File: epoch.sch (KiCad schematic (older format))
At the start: 30 parts, among them J1 USB_OTG, J2 CONN_01X05, P3 CONN_01X10, Q1 DMP1045U, SW1 SW_Reset, SW2 SW_Up, SW3 SW_Middle, SW4 SW_Down, U1 MIC5219-3.3BM5, U2 ATSAMD21Ennc-AU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

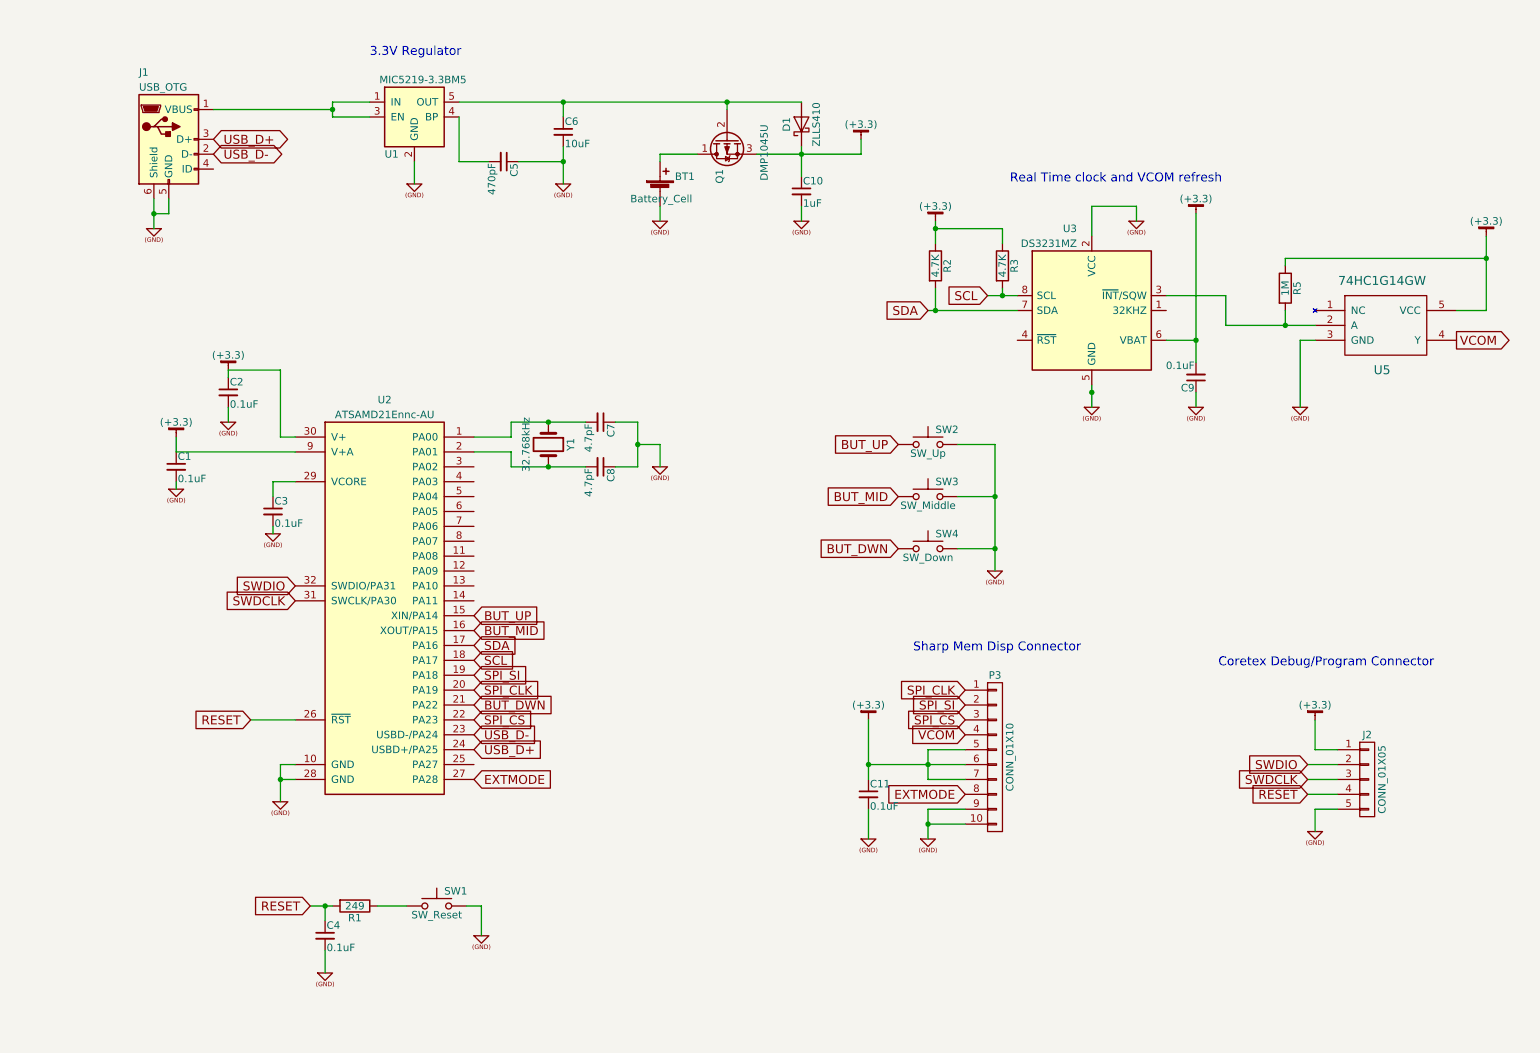
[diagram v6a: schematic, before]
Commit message: Add LIPO charging
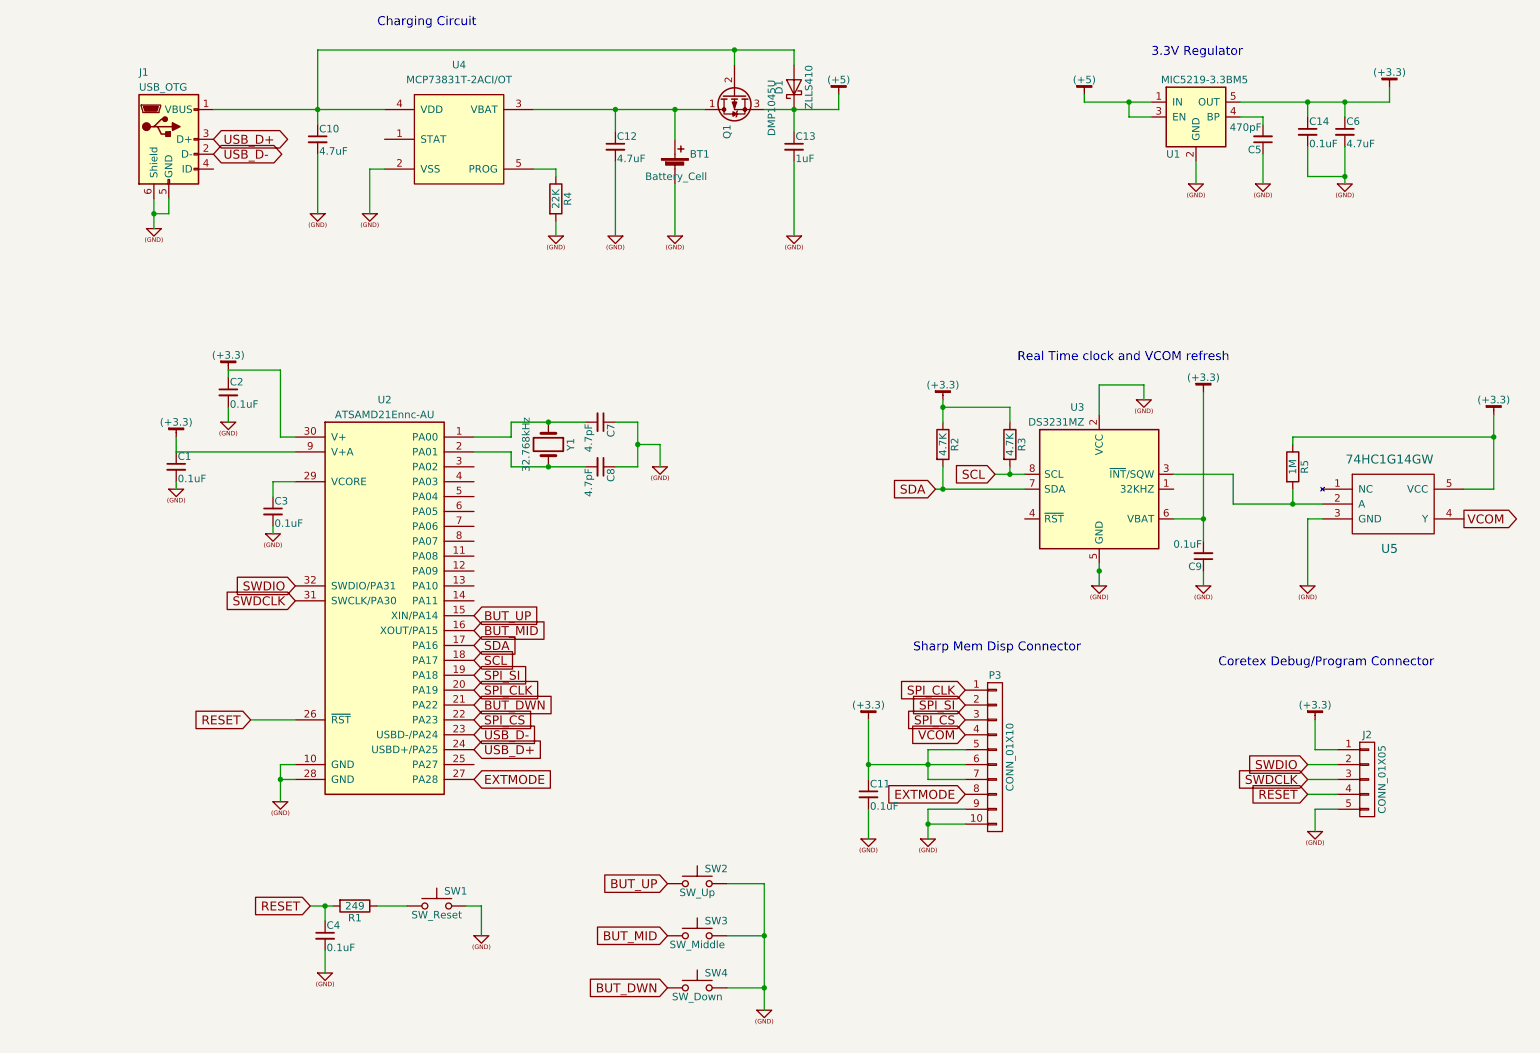
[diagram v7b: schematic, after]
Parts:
- added C12: 4.7uF, Capacitors_SMD:C_0805_HandSoldering, symbol C_Small
- added C13: 1uF, Capacitors_SMD:C_0805_HandSoldering, symbol C_Small
- added C14: 0.1uF, Capacitors_SMD:C_0805_HandSoldering, symbol C_Small
- added R4: 22K, Resistors_SMD:R_0805_HandSoldering, symbol R
- added U4: MCP73831T-2ACI/OT, TO_SOT_Packages_SMD:SOT-23-5_HandSoldering, symbol MCP73831T-2ACI/OT
- C10: value 1uF -> 4.7uF
- C6: value 10uF -> 4.7uF
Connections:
- net (+3.3): now also C6.1, U1.5 (OUT), C14.1; no longer C10.1, D1.1 (K), Q1.3 (S)
- net (GND): now also C12.2, C13.2, C14.2, R4.2, U4.2 (VSS)
- net (+5): now reaches U1.1 (IN), U1.3 (EN)
- net (+5): now also D1.1 (K), Q1.3 (S), C13.1; no longer J1.1 (VBUS)
- net at D1.2 (A), Q1.2 (G): now also C10.1, J1.1 (VBUS), U4.4 (VDD); no longer C6.1, U1.5 (OUT)
- net at BT1.1 (+), Q1.1 (D): now also C12.1, U4.3 (VBAT)
- new net: R4.1, U4.5 (PROG)
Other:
- note added: "Charging Circuit"
- moved on the sheet: C5, C6, C9, R2, R3, R5, SW2, SW3, SW4, U1, U3, U5
